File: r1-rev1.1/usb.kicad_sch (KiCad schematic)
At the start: 13 parts, among them J2 TYPE-C-31-M-12, Q5 AO3401A, U8 USB3320C-EZK

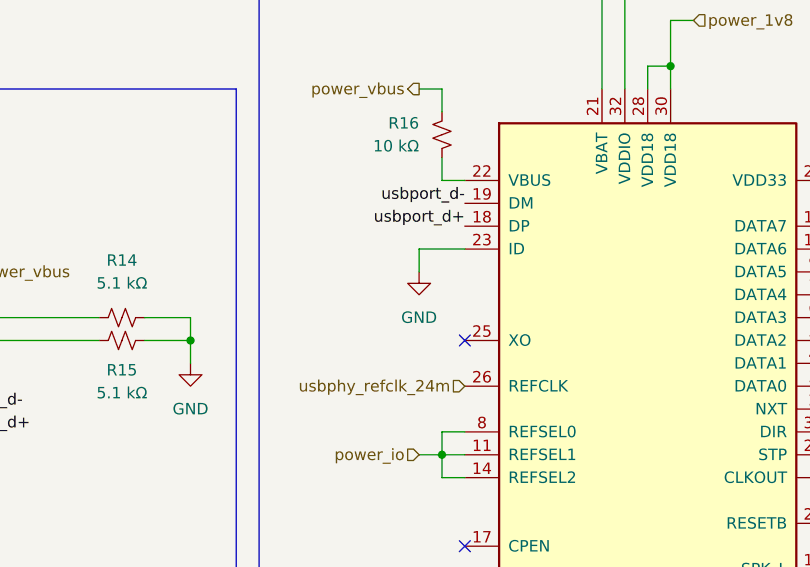
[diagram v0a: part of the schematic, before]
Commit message: Fix USB3320C ID pin
The ID pin should be tied to VDD33 or left floating for
device mode. Tying to ground puts the PHY into host mode,
which requires a software workaround to get USB working.

See Github issue: #9
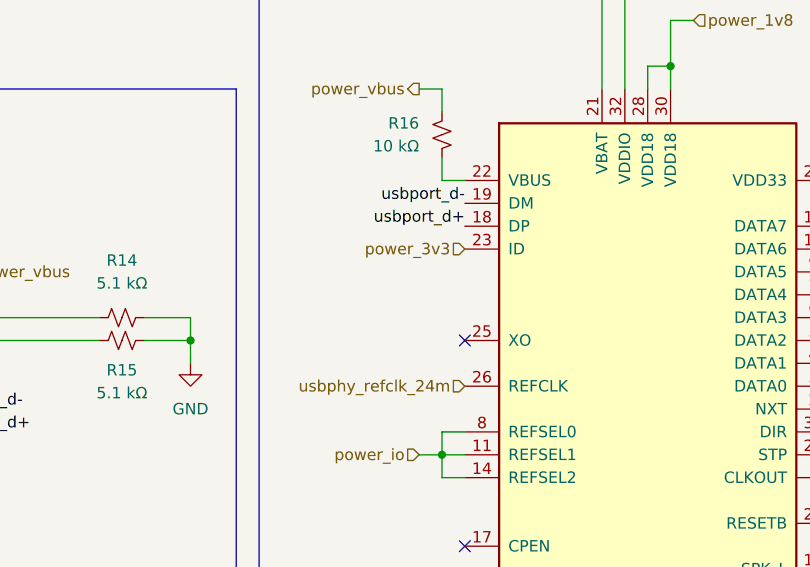
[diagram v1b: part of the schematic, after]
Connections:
- net GND: no longer U8.23 (ID)
- net power_3v3: now also U8.23 (ID)
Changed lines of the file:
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@@
-	(wire
-		(pts
-			(xy 144.78 93.98) (xy 139.7 93.98)
-		)
-		(stroke
-			(width 0)
-			(type default)
-		)
-	)
 	(wire
 		(pts
@@
 		(pts
 			(xy 162.56 63.5) (xy 170.18 63.5)
-		)
-		(stroke
-			(width 0)
-			(type default)
-		)
-	)
-	(wire
-		(pts
-			(xy 139.7 93.98) (xy 139.7 96.52)
 		)
 		(stroke
@@
 			)
 			(justify left)
+		)
+	)
+	(hierarchical_label "power_3v3"
+		(shape input)
+		(at 144.78 93.98 180)
+		(effects
+			(font
+				(size 1.27 1.27)
+			)
+			(justify right)
 		)
 	)
@@
 					(unit 1)
 				)
-			)
-		)
-	)
-	(symbol
-		(lib_id "power:GND")
-		(at 139.7 96.52 0)
-		(unit 1)
-		(exclude_from_sim no)
-		(in_bom yes)
-		(on_board yes)
-		(dnp no)
-		(fields_autoplaced yes)
-		(property "Reference" "#PWR033"
-			(at 139.7 102.87 0)
-			(effects
-				(font
-					(size 1.27 1.27)
-				)
-				(hide yes)
-			)
-		)
-		(property "Value" "GND"
-			(at 139.7 101.6 0)
-			(effects
-				(font
-					(size 1.27 1.27)
-				)
-			)
-		)
-		(property "Footprint" ""
-			(at 139.7 96.52 0)
-			(effects
-				(font
-					(size 1.27 1.27)
-				)
-				(hide yes)
-			)
-		)
-		(property "Datasheet" ""
-			(at 139.7 96.52 0)
-			(effects
-				(font
-					(size 1.27 1.27)
-				)
-				(hide yes)
-			)
-		)
-		(property "Description" "Power symbol creates a global label with name \"GND\" , ground"
-			(at 139.7 96.52 0)
-			(effects
-				(font
-					(size 1.27 1.27)
-				)
-				(hide yes)
-			)
-		)
-		(pin "1"
-		)
-		(instances
-			(project ""
-				(path "/aa241847-30f4-429d-a148-6a6e39ba98e0/2bbed0e1-7a0b-4278-85a9-f432ea240e72"
-					(reference "#PWR033")
-					(unit 1)
-				)

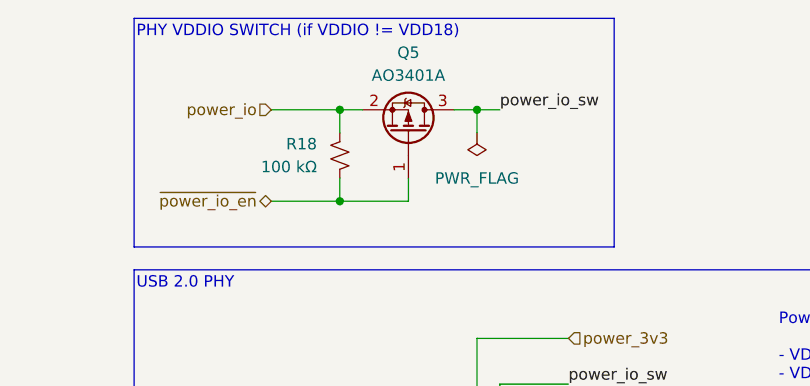
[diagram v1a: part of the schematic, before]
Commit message: Fix symbol library links & resync footprints from KiCAD libraries
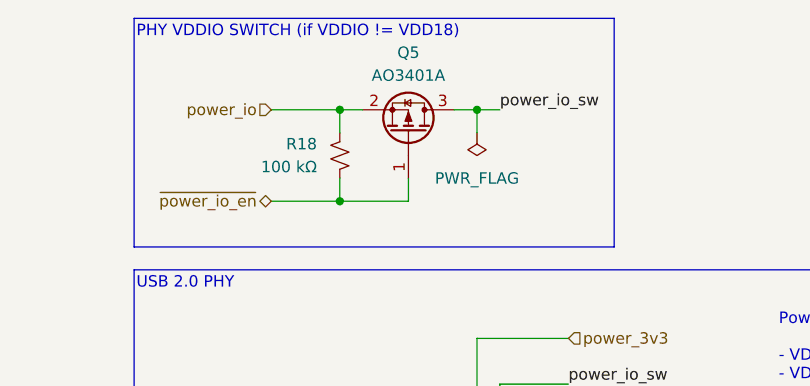
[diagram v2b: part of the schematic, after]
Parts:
- Q5: symbol Device:Q_PMOS_GSD -> Transistor_FET:Q_PMOS_GSD
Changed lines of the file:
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@@
 	)
 	(symbol
-		(lib_id "Device:Q_PMOS_GSD")
+		(lib_id "Transistor_FET:Q_PMOS_GSD")
 		(at 152.4 35.56 270)
 		(mirror x)
